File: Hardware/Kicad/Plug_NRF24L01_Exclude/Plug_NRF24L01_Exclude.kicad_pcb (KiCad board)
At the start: 2 copper layers, 30 x 32.5 mm, 28 parts, among them J1 Conn_01x07_Socket, J2 Conn_01x08_Socket, Q1 2N7002, Q2 2N7002, Q3 2N7002, SW1 SW_Push, U1 STM32L412KBTx, U2 AMS1117-3.3

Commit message: Corrective changes on the Plug_NRF24L01_Exclude KiCad
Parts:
- removed L1: 39n, Inductor_SMD:L_0805_2012Metric_Pad1.05x1.20mm_HandSolder
- removed U2: AMS1117-3.3, Package_TO_SOT_SMD:SOT-223-3_TabPin2
- added C5: 100n, Capacitor_SMD:C_0603_1608Metric_Pad1.08x0.95mm_HandSolder, F.Cu at (140.0, 76.5)
- added C6: 100n, Capacitor_SMD:C_0603_1608Metric_Pad1.08x0.95mm_HandSolder, F.Cu at (140.0, 79.0)
- added D2: LED, Diode_SMD:D_0603_1608Metric_Pad1.05x0.95mm_HandSolder, F.Cu at (167.1, 102.0)
- added J3: Conn_02x07_Odd_Even, Connector_PinHeader_1.27mm:PinHeader_2x07_P1.27mm_Vertical_SMD, F.Cu at (160.1, 97.3)
- added Q4: 2N7002, Package_TO_SOT_SMD:SOT-23, F.Cu at (167.3, 94.0)
- added Q5: 2N7002, Package_TO_SOT_SMD:SOT-23, F.Cu at (167.3, 98.5)
- added R11: 10k, Resistor_SMD:R_0603_1608Metric_Pad0.98x0.95mm_HandSolder, F.Cu at (153.1, 95.6)
- added R12: 10k, Resistor_SMD:R_0603_1608Metric_Pad0.98x0.95mm_HandSolder, F.Cu at (153.1, 98.1)
- added R13: 10k, Resistor_SMD:R_0603_1608Metric_Pad0.98x0.95mm_HandSolder, F.Cu at (153.1, 100.6)
- added R15: 1k, Resistor_SMD:R_0603_1608Metric_Pad0.98x0.95mm_HandSolder, F.Cu at (153.1, 103.1)
- added R2: 10k, Resistor_SMD:R_0603_1608Metric_Pad0.98x0.95mm_HandSolder, F.Cu at (153.1, 93.1)
- added U3: MIC5219-3.3YMM, Package_SO:MSOP-8_3x3mm_P0.65mm, F.Cu at (145.9, 70.0)
- C1: value 1u -> 470p
- C2: value 1u -> 2.2u
- C3: value 1u -> 100n
- C4: value 10n -> 100n
- J1: footprint Connector_PinSocket_1.00mm:PinSocket_1x07_P1.00mm_Vertical -> Connector_JST:JST_SUR_SM08B-SURS-TF_1x08-1MP_P0.80mm_Horizontal
- moved C3 37.3 mm to (140.0, 71.5)
- moved C4 36.6 mm to (140.0, 74.0)
- moved C1 23.4 mm to (140.0, 69.0), turned to 0 degrees
- moved J1 12.7 mm to (130.4, 71.6)
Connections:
- net Serial_Data_SNES renamed Serial_Data1_SNES
- net Serial_Data_STM32 renamed Serial_Data1_STM32
- C1 pad 1: +5V -> Net-(U3-BP)
- C3 pad 1: +3.3VA -> GND
- C3 pad 2: GND -> NRST
- C4 pad 1: +3.3VA -> +3.3V
- J1 pad 5: unconnected-(J1-Pin_5-Pad5) -> Serial_Data2_SNES
- J1 pad 6: unconnected-(J1-Pin_6-Pad6) -> IOBit_SNES
- U1 pad 12: unconnected-(U1-PA6-Pad12) -> SPI_Digital_Input
- U1 pad 20: unconnected-(U1-PA10-Pad20) -> Player1_LED
- U1 pad 23: unconnected-(U1-PA13-Pad23) -> SWDIO
- U1 pad 24: Player1_LED -> SWDCK
- U1 pad 28: unconnected-(U1-PB5-Pad28) -> Serial_Data2_SNES
- U1 pad 30: unconnected-(U1-PB7-Pad30) -> IOBit_SNES
- U1 pad 4: unconnected-(U1-NRST-Pad4) -> NRST
- U1 pad 5: +3.3VA -> +3.3V
- U1 pad 6: unconnected-(U1-PA0-Pad6) -> SPI_Clock
- U1 pad 8: SPI_Digital_Input -> USART2_TX
- U1 pad 9: SPI_Clock -> USART2_RX
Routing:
- net +3.3VA: track 13.1 -> 0.00 mm, vias 2 -> 0
- net +3.3V: track 70.7 -> 83.8 mm, vias 6 -> 8

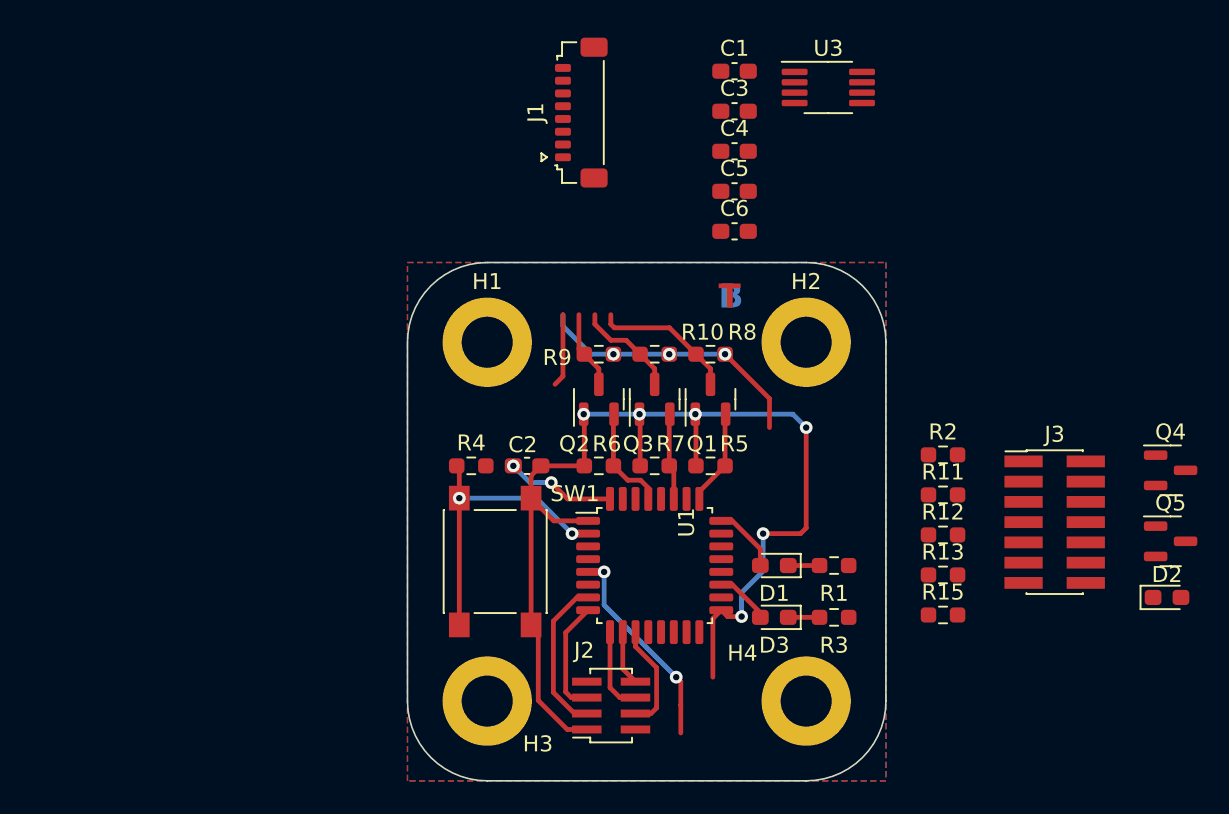
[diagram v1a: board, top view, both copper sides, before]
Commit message: Updated Plug_NRF24L01_Exclude (Version 1.0) - Schematic (New pins assignment / New buttons) - PCB (Completed Routing V1)
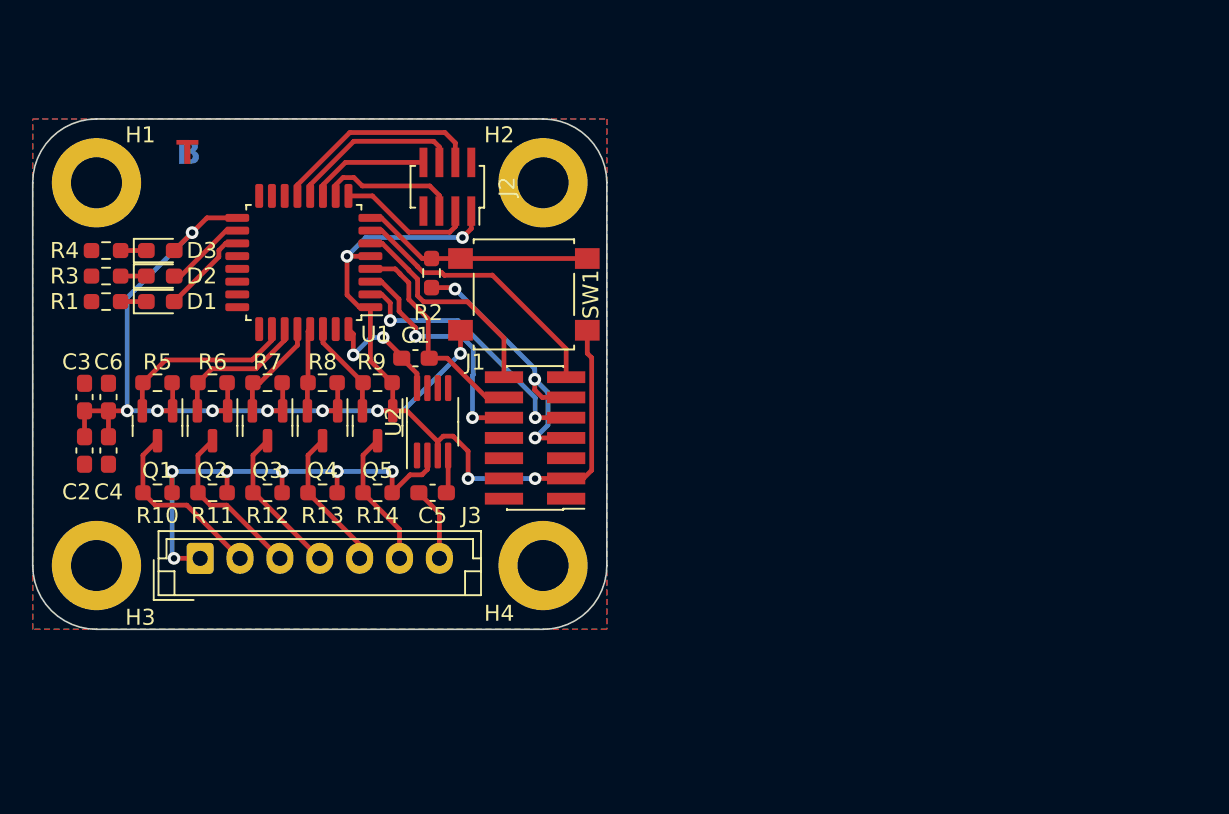
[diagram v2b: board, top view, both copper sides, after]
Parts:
- removed R15: 1k, Resistor_SMD:R_0603_1608Metric_Pad0.98x0.95mm_HandSolder
- removed U3: MIC5219-3.3YMM, Package_SO:MSOP-8_3x3mm_P0.65mm
- added R14: 10k, Resistor_SMD:R_0603_1608Metric_Pad0.98x0.95mm_HandSolder, F.Cu at (117.6, 95.4)
- added U2: MIC5219-3.3YMM, Package_SO:MSOP-8_3x3mm_P0.65mm, F.Cu at (121.1, 91.0)
- C1: value 470p -> 100n
- C2: value 2.2u -> 100n
- C5: value 100n -> 470p
- C6: value 100n -> 2.2u
- D2: value LED -> LED_Small
- D3: value LED_Small -> LED
- J1: value Conn_01x07_Socket -> Conn_02x07_Odd_Even; footprint Connector_JST:JST_SUR_SM08B-SURS-TF_1x08-1MP_P0.80mm_Horizontal -> Connector_PinHeader_1.27mm:PinHeader_2x07_P1.27mm_Vertical_SMD
- J3: value Conn_02x07_Odd_Even -> Conn_01x07_Socket; footprint Connector_PinHeader_1.27mm:PinHeader_2x07_P1.27mm_Vertical_SMD -> Connector_JST:JST_EH_B7B-EH-A_1x07_P2.50mm_Vertical
- R4: value 10k -> 1k
- SW1: value SW_Push -> SW_SPST; footprint Button_Switch_SMD:SW_Push_1P1T_NO_6x6mm_H9.5mm -> Button_Switch_SMD:SW_SPST_B3S-1000
- moved D2 66.3 mm to (104.0, 81.8)
- moved J3 53.6 mm to (106.5, 99.5)
- moved Q4 53.2 mm to (114.2, 91.2), turned to -90 degrees
- moved R3 50.4 mm to (100.6, 81.8), turned to 180 degrees
- moved Q5 50.2 mm to (117.6, 91.2), turned to -90 degrees
- moved R1 48.6 mm to (100.6, 83.5), turned to 180 degrees
- moved R11 45.8 mm to (107.3, 95.4), turned to 180 degrees
- moved D3 44.8 mm to (104.0, 80.2), turned to 0 degrees
- moved C3 44.5 mm to (99.2, 89.4), turned to 90 degrees
- moved C4 43.5 mm to (100.8, 92.8), turned to -90 degrees
- moved R12 42.4 mm to (110.7, 95.4), turned to 180 degrees
- moved D1 41.9 mm to (104.0, 83.5), turned to 0 degrees
- moved C6 40.6 mm to (100.8, 89.4), turned to 90 degrees
- moved R13 39.2 mm to (114.2, 95.4), turned to 180 degrees
- moved R5 35.1 mm to (103.8, 88.5), turned to 180 degrees
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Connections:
- C1 pad 1: Net-(U3-BP) -> GND
- C1 pad 2: GND -> NRST
- C3 pad 1: GND -> +3.3V
- C3 pad 2: NRST -> GND
- C5 pad 1: +3.3V -> Net-(U2-BP)
- D2 pad 2: +3.3V -> Status_LED
- D3 pad 2: Status_LED -> +3.3V
- J1 pad 1: +5V -> unconnected-(J1-Pin_1-Pad1)
- J1 pad 2: Data_Clock_SNES -> unconnected-(J1-Pin_2-Pad2)
- J1 pad 3: Data_Latch_SNES -> +3.3V
- J1 pad 4: Serial_Data1_SNES -> unconnected-(J1-Pin_4-Pad4)
- J1 pad 5: Serial_Data2_SNES -> GND
- J1 pad 6: IOBit_SNES -> unconnected-(J1-Pin_6-Pad6)
- J1 pad 8: (no net) -> unconnected-(J1-Pin_8-Pad8)
- J3 pad 1: unconnected-(J3-Pin_1-Pad1) -> +5V
- J3 pad 2: unconnected-(J3-Pin_2-Pad2) -> Data_Clock_SNES
- J3 pad 3: +3.3V -> Data_Latch_SNES
- J3 pad 4: SWDIO -> Serial_Data1_SNES
- J3 pad 5: GND -> Serial_Data2_SNES
- J3 pad 6: SWDCK -> IOBit_SNES
- Q1 pad 2: Serial_Data1_STM32 -> Data_Clock_STM32
- Q1 pad 3: Serial_Data1_SNES -> Data_Clock_SNES
- Q2 pad 2: Data_Clock_STM32 -> Data_Latch_STM32
- Q2 pad 3: Data_Clock_SNES -> Data_Latch_SNES
- Q3 pad 2: Data_Latch_STM32 -> Serial_Data1_STM32
- Q3 pad 3: Data_Latch_SNES -> Serial_Data1_SNES
- Q4 pad 2: IOBit_STM32 -> Serial_Data2_STM32
- Q4 pad 3: IOBit_SNES -> Serial_Data2_SNES
- Q5 pad 2: Serial_Data2_STM32 -> IOBit_STM32
- Q5 pad 3: Serial_Data2_SNES -> IOBit_SNES
- R10 pad 2: Data_Latch_SNES -> Data_Clock_SNES
- R11 pad 2: IOBit_SNES -> Data_Latch_SNES
- R12 pad 1: +3.3V -> +5V
- R12 pad 2: Serial_Data2_STM32 -> Serial_Data1_SNES
- R2 pad 1: +3.3V -> Appairing_Btn
- R2 pad 2: IOBit_STM32 -> GND
- R3 pad 1: Net-(D3-K) -> Net-(D2-K)
- R4 pad 1: Appairing_Btn -> Net-(D3-K)
- R5 pad 2: Serial_Data1_STM32 -> Data_Clock_STM32
- R6 pad 2: Data_Clock_STM32 -> Data_Latch_STM32
- R7 pad 2: Data_Latch_STM32 -> Serial_Data1_STM32
- R8 pad 1: +5V -> +3.3V
- R8 pad 2: Serial_Data1_SNES -> Serial_Data2_STM32
- R9 pad 1: +5V -> +3.3V
- R9 pad 2: Data_Clock_SNES -> IOBit_STM32
- SW1 pad 1: +3.3V -> Appairing_Btn
- SW1 pad 2: Appairing_Btn -> +3.3V
- U1 pad 10: SPI_Digital_Output -> SPI_Digital_Input
- U1 pad 11: Chip_Enable -> SPI_Digital_Output
- U1 pad 12: SPI_Digital_Input -> SPI_Clock
- U1 pad 13: unconnected-(U1-PA7-Pad13) -> Chip_Enable
- U1 pad 18: unconnected-(U1-PA8-Pad18) -> Status_LED
- U1 pad 19: Status_LED -> Player1_LED
- U1 pad 2: Appairing_Btn -> SWDIO
- U1 pad 20: Player1_LED -> unconnected-(U1-PA10-Pad20)
- U1 pad 23: SWDIO -> unconnected-(U1-PA13-Pad23)
- U1 pad 24: SWDCK -> unconnected-(U1-PA14-Pad24)
- U1 pad 25: Serial_Data1_STM32 -> unconnected-(U1-PA15-Pad25)
- U1 pad 26: unconnected-(U1-PB3-Pad26) -> Data_Clock_STM32
- U1 pad 28: Serial_Data2_SNES -> Serial_Data1_STM32
- U1 pad 29: Data_Clock_STM32 -> Serial_Data2_STM32
- U1 pad 3: unconnected-(U1-PC15-Pad3) -> SWDCK
- U1 pad 30: IOBit_SNES -> IOBit_STM32
- U1 pad 6: SPI_Clock -> USART2_TX
- U1 pad 7: SPI_Chip_Select -> USART2_RX
- U1 pad 8: USART2_TX -> Appairing_Btn
- U1 pad 9: USART2_RX -> SPI_Chip_Select
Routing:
- net GND: track 6.92 -> 31.2 mm, vias 2 -> 5
- net +3.3V: track 83.8 -> 107.2 mm, vias 8 -> 12
- net USART2_RX: track 0.00 -> 17.1 mm
- net SWDIO: track 0.00 -> 16.9 mm, vias 0 -> 2
- net SWDCK: track 0.00 -> 15.3 mm, vias 0 -> 2
- net USART2_TX: track 0.00 -> 13.9 mm
- net NRST: track 0.00 -> 13.7 mm
- net +5V: track 21.9 -> 31.3 mm, vias 3 -> 6
- net Serial_Data2_SNES: track 0.00 -> 9.09 mm
- net IOBit_SNES: track 0.00 -> 8.70 mm
- net Chip_Enable: track 6.77 -> 13.4 mm
- net Data_Clock_SNES: track 4.88 -> 11.4 mm
- net IOBit_STM32: track 0.00 -> 6.18 mm
- net SPI_Clock: track 5.34 -> 11.0 mm
- net Serial_Data2_STM32: track 0.00 -> 5.20 mm
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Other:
- board size 30 x 32.5 mm -> 36 x 32 mm

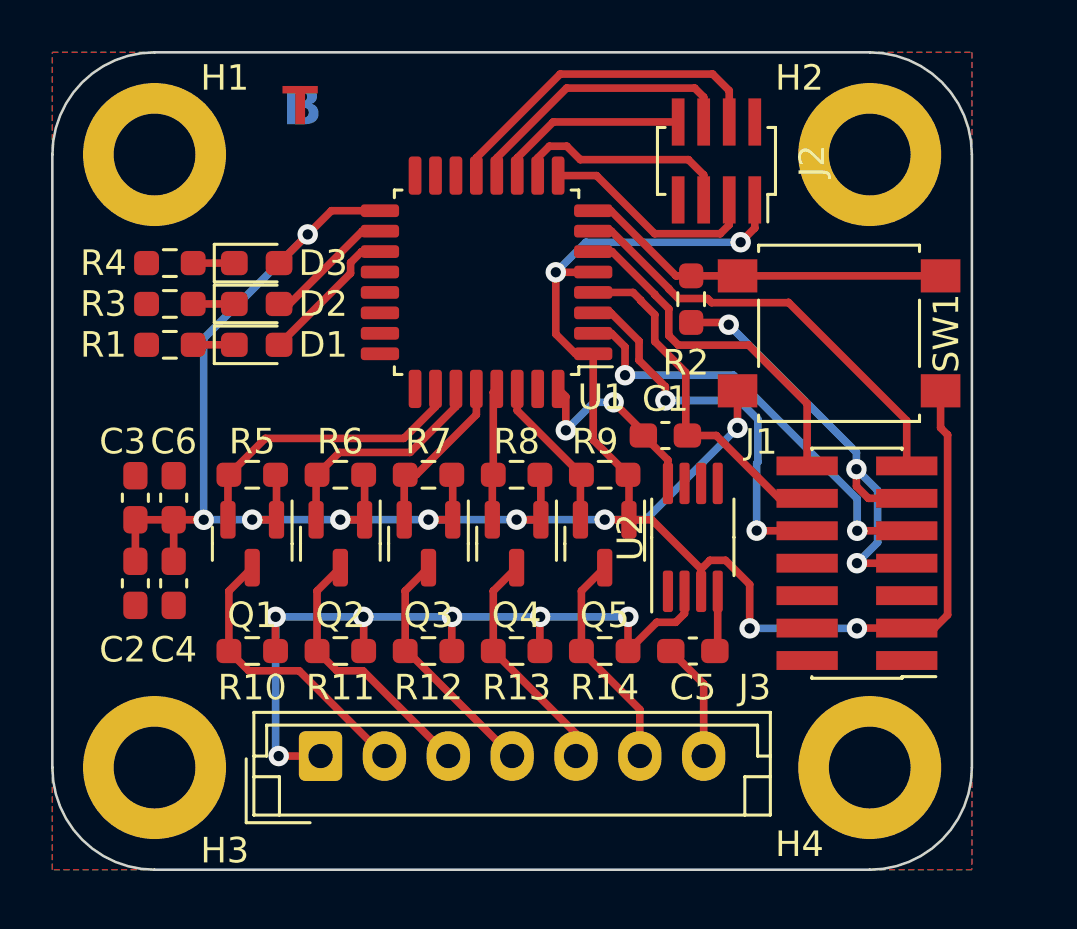
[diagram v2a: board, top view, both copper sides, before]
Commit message: Updated Plug_NRF24L01_Exclude (V1.1) - PCB (Routing) / Schematic (Pins assignment)
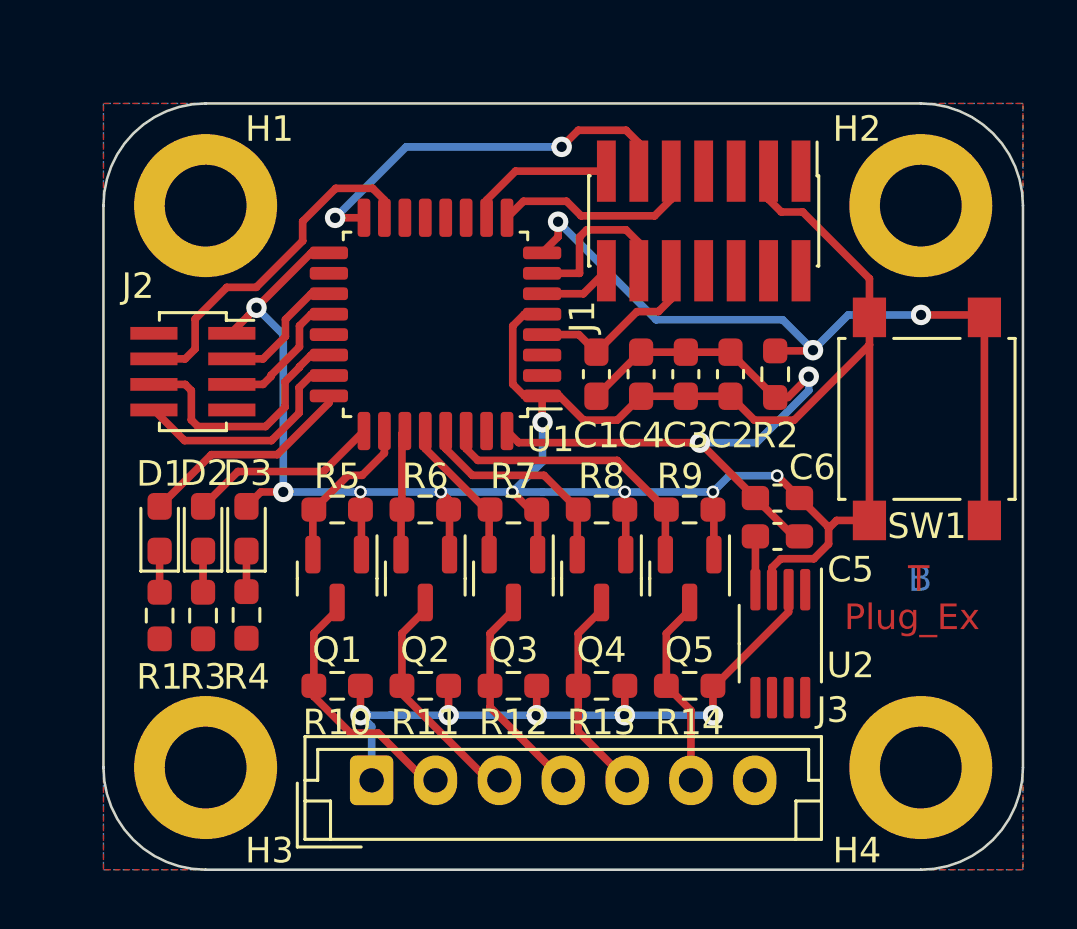
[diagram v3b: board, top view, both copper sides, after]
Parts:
- moved C2 24.7 mm to (122.5, 84.6), turned to 90 degrees
- moved C6 23.6 mm to (124.4, 89.5), turned to 180 degrees
- moved J2 22.1 mm to (101.5, 84.5), turned to 0 degrees
- moved C3 22.1 mm to (120.8, 84.6)
- moved C4 20.0 mm to (119.0, 84.6), turned to 90 degrees
- moved J1 14.7 mm to (121.5, 78.6), turned to -90 degrees
- moved R4 14.1 mm to (103.6, 94.0), turned to -90 degrees
- moved R3 12.3 mm to (101.9, 94.0), turned to -90 degrees
- moved R1 10.6 mm to (100.2, 94.0), turned to -90 degrees
- moved D3 10.4 mm to (103.6, 90.7), turned to 90 degrees
- moved D2 9.05 mm to (101.9, 90.7), turned to 90 degrees
- moved D1 8.14 mm to (100.2, 90.7), turned to 90 degrees
- moved C5 5.58 mm to (124.4, 91.0), turned to 0 degrees
- moved U2 5.39 mm to (124.5, 95.2), turned to -90 degrees
- moved SW1 4.80 mm to (130.2, 86.3), turned to -90 degrees
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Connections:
- J1 pad 10: SWDCK -> NRST
- J1 pad 12: NRST -> USART2_RX
- J1 pad 13: USART2_RX -> SWDCK
- U1 pad 10: SPI_Digital_Input -> SWDCK
- U1 pad 11: SPI_Digital_Output -> unconnected-(U1-PA5-Pad11)
- U1 pad 12: SPI_Clock -> unconnected-(U1-PA6-Pad12)
- U1 pad 13: Chip_Enable -> unconnected-(U1-PA7-Pad13)
- U1 pad 15: unconnected-(U1-PB1-Pad15) -> Chip_Enable
- U1 pad 18: Status_LED -> unconnected-(U1-PA8-Pad18)
- U1 pad 19: Player1_LED -> SPI_Chip_Select
- U1 pad 2: SWDIO -> unconnected-(U1-PC14-Pad2)
- U1 pad 20: unconnected-(U1-PA10-Pad20) -> SPI_Digital_Input
- U1 pad 22: unconnected-(U1-PA12-Pad22) -> SPI_Clock
- U1 pad 23: unconnected-(U1-PA13-Pad23) -> SPI_Digital_Output
- U1 pad 24: unconnected-(U1-PA14-Pad24) -> Player1_LED
- U1 pad 25: unconnected-(U1-PA15-Pad25) -> Status_LED
- U1 pad 3: SWDCK -> unconnected-(U1-PC15-Pad3)
- U1 pad 9: SPI_Chip_Select -> SWDIO
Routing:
- net Appairing_Btn: track 14.7 -> 30.3 mm, vias 0 -> 3
- net GND: track 31.2 -> 44.7 mm, vias 5 -> 4
- net USART2_TX: track 13.9 -> 2.89 mm
- net USART2_RX: track 17.1 -> 6.63 mm
- net +3.3V: track 107.2 -> 97.7 mm, vias 12 -> 9
- net SWDCK: track 15.3 -> 5.85 mm, vias 2 -> 0
- net SWDIO: track 16.9 -> 8.30 mm, vias 2 -> 0
- net NRST: track 13.7 -> 7.30 mm
- net Data_Clock_STM32: track 11.7 -> 6.32 mm
- net IOBit_STM32: track 6.18 -> 11.3 mm
- net Data_Latch_STM32: track 9.01 -> 4.90 mm
- net +5V: track 31.3 -> 27.3 mm, vias 6 -> 5
- net SPI_Chip_Select: track 8.76 -> 5.25 mm
- net Serial_Data2_STM32: track 5.20 -> 8.64 mm
- net SPI_Digital_Input: track 8.82 -> 5.45 mm
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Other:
- board size 36 x 32 mm -> 36 x 30 mm
- board text added: "Plug_Ex"

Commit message: Update PCB
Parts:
- moved C2 4.69 mm to (118.0, 85.8), turned to 0 degrees
- moved C4 2.71 mm to (121.5, 85.8), turned to 0 degrees
- moved C1 0.78 mm to (118.0, 84.2), turned to 180 degrees
- moved C3 0.78 mm to (121.5, 84.2), turned to 0 degrees
- moved R2 0.40 mm to (124.2, 85.0), turned to 90 degrees
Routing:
- net GND: track 44.7 -> 28.9 mm, vias 4 -> 3
- net +3.3V: track 97.7 -> 82.5 mm
- net NRST: track 7.30 -> 0.00 mm
- net Appairing_Btn: track 30.3 -> 27.8 mm
